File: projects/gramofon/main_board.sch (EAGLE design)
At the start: 2 parts

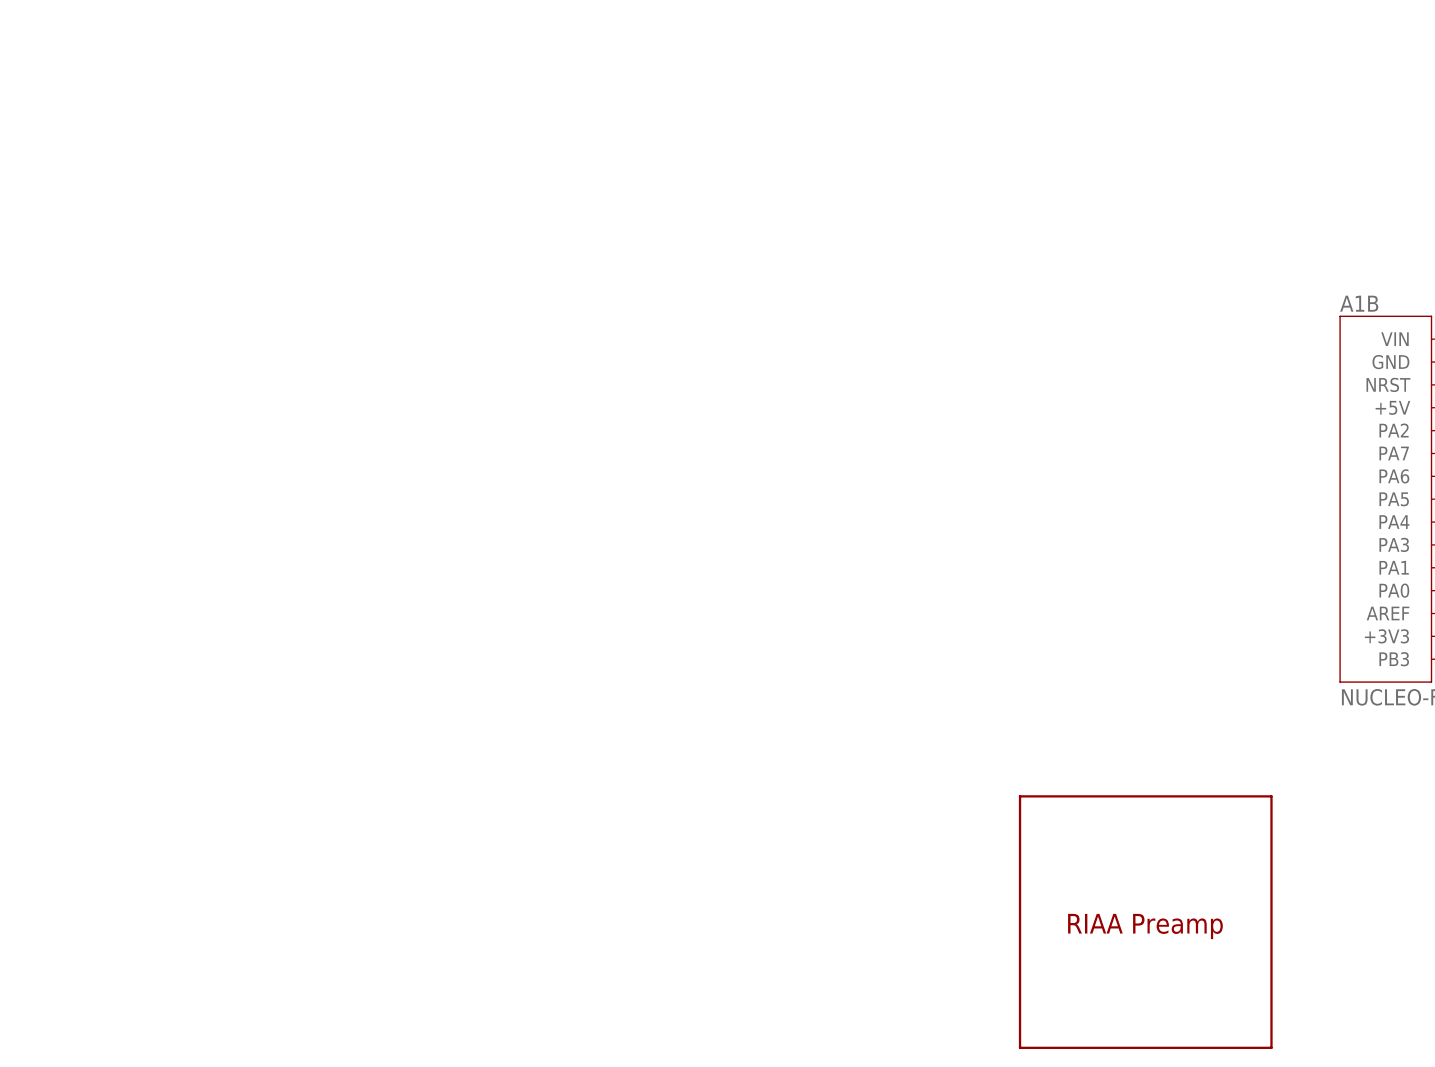
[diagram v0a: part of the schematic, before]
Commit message: fixed waldek missing pwm outputs, wop on gramofon
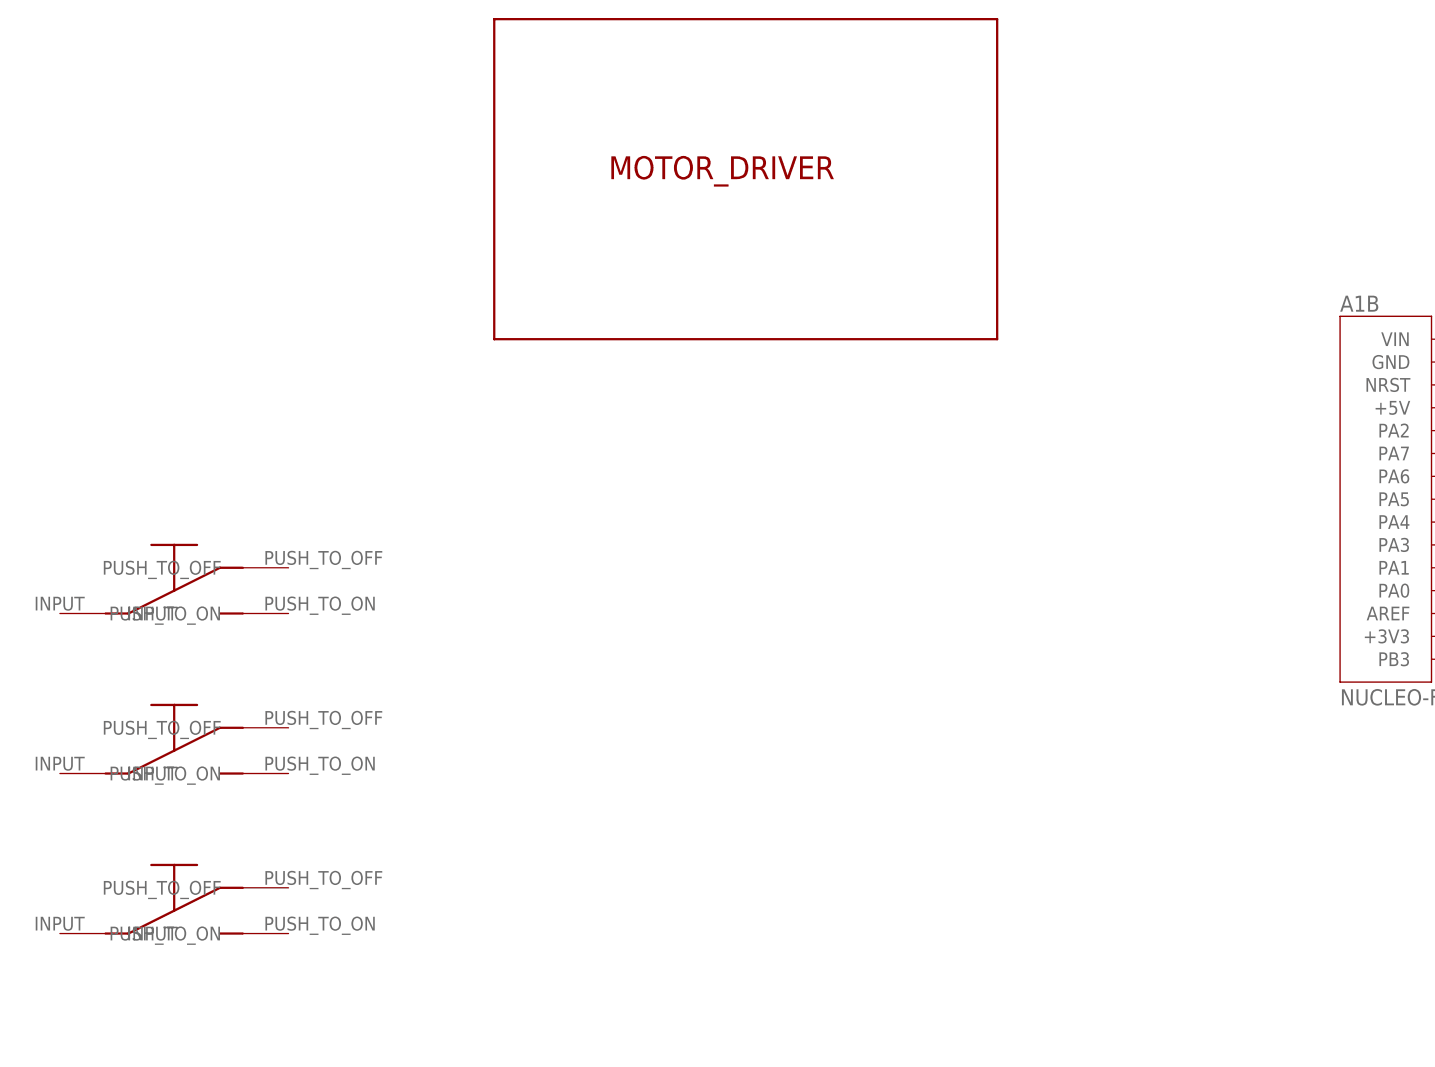
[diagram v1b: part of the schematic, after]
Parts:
- removed U$1: RIAA_PREAMP, ligocki:RIAA_PREAMP
- added U$2, U$3, U$4: BUTTON, gramofon:BUTTON
- added U$5: MOTOR_DRIVER, gramofon:MOTOR_DRIVER
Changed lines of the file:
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@@
 <?xml version="1.0" encoding="utf-8"?>
 <!DOCTYPE eagle SYSTEM "eagle.dtd">
-<eagle version="9.3.2">
+<eagle version="9.6.2">
 <drawing>
 <settings>
@@
 </classes>
 <parts>
-<part name="U$1" library="ligocki" deviceset="RIAA_PREAMP" device=""/>
 <part name="A1" library="NUCLEO-F303K8" deviceset="NUCLEO-F303K8" device=""/>
+<part name="U$2" library="gramofon" deviceset="BUTTON" device=""/>
+<part name="U$3" library="gramofon" deviceset="BUTTON" device=""/>
+<part name="U$4" library="gramofon" deviceset="BUTTON" device=""/>
+<part name="U$5" library="gramofon" deviceset="MOTOR_DRIVER" device=""/>
 </parts>
 <sheets>
@@
 </plain>
 <instances>
-<instance part="U$1" gate="G$1" x="10.16" y="7.62" smashed="yes"/>
 <instance part="A1" gate="A" x="71.12" y="68.58" smashed="yes">
 <attribute name="NAME" x="66.03081875" y="89.4456" size="1.781209375" layer="95"/>
@@
 <attribute name="VALUE" x="45.710990625" y="45.6795" size="1.78115" layer="96"/>
 </instance>
+<instance part="U$2" gate="G$1" x="-99.06" y="55.88" smashed="yes"/>
+<instance part="U$3" gate="G$1" x="-99.06" y="38.1" smashed="yes"/>
+<instance part="U$4" gate="G$1" x="-99.06" y="20.32" smashed="yes"/>
+<instance part="U$5" gate="G$1" x="-20.32" y="104.14" smashed="yes"/>
 </instances>
 <busses>

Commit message: updated gramofon board
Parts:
- added C1, C3, C4, C5: 100n, rcl:C-EUC1206
- added C2: 100u, rcl:CPOL-EU150CLZ-1010
- added LED1: (no value), led:LEDSMT1206
- added R1, R2, R3, R4: 10k, rcl:R-EU_R1206
- added X1, X2, X3, X4, X5, X6, X7, X8: (no value), con-wago-500:W237-102
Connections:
- new net 3V3: A1B.+3V3, X6-1.KL
- new net ADC_0: A1B.PA5, X2-2.KL
- new net ADC_1: A1B.PA4, X2-1.KL
- new net BUTT_0: C5.1, R2.1, U$4.INPUT
- new net BUTT_1: C4.1, R3.1, U$2.INPUT
- new net BUTT_2: C3.1, R4.1, U$3.INPUT
- new net GND: A1A.GND, A1B.GND, C1.2, C2.-, C3.2, C4.2, C5.2, LED1.C, U$2.PUSH_TO_ON, U$3.PUSH_TO_ON, U$4.PUSH_TO_ON, X1-2.KL, X5-2.KL, X6-2.KL, X7-1.KL, X7-2.KL, X8-1.KL, X8-2.KL
- new net IO_0: A1B.PA1, X4-2.KL
- new net IO_1: A1B.PA0, X4-1.KL
- new net N$8: LED1.A, R1.1
- new net PWM_0: A1B.PA7, X3-2.KL
- new net PWM_1: A1B.PA6, X3-1.KL
- new net VCC: A1B.+5V, A1B.VIN, C1.1, C2.+, R1.2, R2.2, R3.2, R4.2, X1-1.KL, X5-1.KL
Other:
- moved on the sheet: A1A, A1B

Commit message: upgraded gramofon board
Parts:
- added X10, X11: (no value), con-wago-500:W237-102
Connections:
- new net IO_2: A1A.PB4, X11-2.KL
- new net IO_3: A1A.PB5, X11-1.KL
- new net POT: A1B.PA3
- new net PWM_2: A1A.PA9, X10-2.KL
- new net PWM_3: A1A.PA10, X10-1.KL
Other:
- moved on the sheet: A1A
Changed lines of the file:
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@@
 <part name="X8" library="con-wago-500" library_urn="urn:adsk.eagle:library:195" deviceset="W237-102" device="" package3d_urn="urn:adsk.eagle:package:10688/1"/>
 <part name="GND6" library="supply1" library_urn="urn:adsk.eagle:library:371" deviceset="GND" device=""/>
+<part name="X10" library="con-wago-500" library_urn="urn:adsk.eagle:library:195" deviceset="W237-102" device="" package3d_urn="urn:adsk.eagle:package:10688/1"/>
+<part name="X11" library="con-wago-500" library_urn="urn:adsk.eagle:library:195" deviceset="W237-102" device="" package3d_urn="urn:adsk.eagle:package:10688/1"/>
 </parts>
 <sheets>
@@
 </plain>
 <instances>
-<instance part="A1" gate="A" x="0" y="68.58" smashed="yes">
-<attribute name="NAME" x="-5.08918125" y="89.4456" size="1.781209375" layer="95"/>
-<attribute name="VALUE" x="-5.083259375" y="45.9595" size="1.779140625" layer="96"/>
+<instance part="A1" gate="A" x="35.56" y="68.58" smashed="yes" rot="MR0">
+<attribute name="NAME" x="40.64918125" y="89.4456" size="1.781209375" layer="95" rot="MR0"/>
+<attribute name="VALUE" x="40.643259375" y="45.9595" size="1.779140625" layer="96" rot="MR0"/>
 </instance>
 <instance part="A1" gate="B" x="55.88" y="68.58" smashed="yes">
@@
 <instance part="GND6" gate="1" x="116.84" y="30.48" smashed="yes">
 <attribute name="VALUE" x="114.3" y="27.94" size="1.778" layer="96"/>
+</instance>
+<instance part="X10" gate="-1" x="124.46" y="81.28" smashed="yes" rot="R180">
+<attribute name="NAME" x="124.46" y="80.391" size="1.778" layer="95"/>
+</instance>
+<instance part="X10" gate="-2" x="124.46" y="86.36" smashed="yes" rot="R180">
+<attribute name="VALUE" x="127" y="90.043" size="1.778" layer="96" rot="R180"/>
+<attribute name="NAME" x="124.46" y="85.471" size="1.778" layer="95"/>
+</instance>
+<instance part="X11" gate="-1" x="124.46" y="58.42" smashed="yes" rot="R180">
+<attribute name="NAME" x="124.46" y="57.531" size="1.778" layer="95"/>
+</instance>
+<instance part="X11" gate="-2" x="124.46" y="63.5" smashed="yes" rot="R180">
+<attribute name="VALUE" x="127" y="67.183" size="1.778" layer="96" rot="R180"/>
+<attribute name="NAME" x="124.46" y="62.611" size="1.778" layer="95"/>
 </instance>
 </instances>
@@
 <pinref part="A1" gate="A" pin="GND"/>
 <pinref part="GND2" gate="1" pin="GND"/>
-<wire x1="10.16" y1="78.74" x2="17.78" y2="78.74" width="0.1524" layer="91"/>
+<wire x1="25.4" y1="78.74" x2="17.78" y2="78.74" width="0.1524" layer="91"/>
 <wire x1="17.78" y1="78.74" x2="17.78" y2="43.18" width="0.1524" layer="91"/>
 </segment>
@@
 </segment>
 </net>
+<net name="PWM_2" class="0">
+<segment>
+<pinref part="X10" gate="-2" pin="KL"/>
+<wire x1="119.38" y1="86.36" x2="101.6" y2="86.36" width="0.1524" layer="91"/>
+<label x="106.68" y="86.36" size="1.778" layer="95"/>
+</segment>
+<segment>
+<pinref part="A1" gate="A" pin="PA9"/>
+<wire x1="25.4" y1="86.36" x2="5.08" y2="86.36" width="0.1524" layer="91"/>
+<label x="10.16" y="86.36" size="1.778" layer="95"/>
+</segment>
+</net>
+<net name="PWM_3" class="0">
+<segment>
+<pinref part="X10" gate="-1" pin="KL"/>
+<wire x1="119.38" y1="81.28" x2="101.6" y2="81.28" width="0.1524" layer="91"/>
+<label x="106.68" y="81.28" size="1.778" layer="95"/>
+</segment>
+<segment>
+<pinref part="A1" gate="A" pin="PA10"/>
+<wire x1="25.4" y1="83.82" x2="5.08" y2="83.82" width="0.1524" layer="91"/>
+<label x="10.16" y="83.82" size="1.778" layer="95"/>
+</segment>
+</net>
+<net name="IO_2" class="0">
+<segment>
+<pinref part="X11" gate="-2" pin="KL"/>
+<wire x1="119.38" y1="63.5" x2="101.6" y2="63.5" width="0.1524" layer="91"/>
+<label x="106.68" y="63.5" size="1.778" layer="95"/>
+</segment>
+<segment>
+<pinref part="A1" gate="A" pin="PB4"/>
+<wire x1="25.4" y1="50.8" x2="2.54" y2="50.8" width="0.1524" layer="91"/>
+<label x="5.08" y="50.8" size="1.778" layer="95"/>
+</segment>
+</net>
+<net name="IO_3" class="0">
+<segment>
+<pinref part="X11" gate="-1" pin="KL"/>
+<wire x1="119.38" y1="58.42" x2="101.6" y2="58.42" width="0.1524" layer="91"/>
+<label x="106.68" y="58.42" size="1.778" layer="95"/>
+</segment>
+<segment>
+<pinref part="A1" gate="A" pin="PB5"/>
+<wire x1="25.4" y1="53.34" x2="2.54" y2="53.34" width="0.1524" layer="91"/>
+<label x="5.08" y="53.34" size="1.778" layer="95"/>
+</segment>
+</net>
+<net name="POT" class="0">
+<segment>
+<pinref part="A1" gate="B" pin="PA3"/>
+<wire x1="66.04" y1="63.5" x2="86.36" y2="63.5" width="0.1524" layer="91"/>
+<label x="76.2" y="63.5" size="1.778" layer="95"/>
+</segment>
+</net>
